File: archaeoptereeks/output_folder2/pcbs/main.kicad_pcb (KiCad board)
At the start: 2 copper layers, 246.9 x 153.3 mm, 118 parts

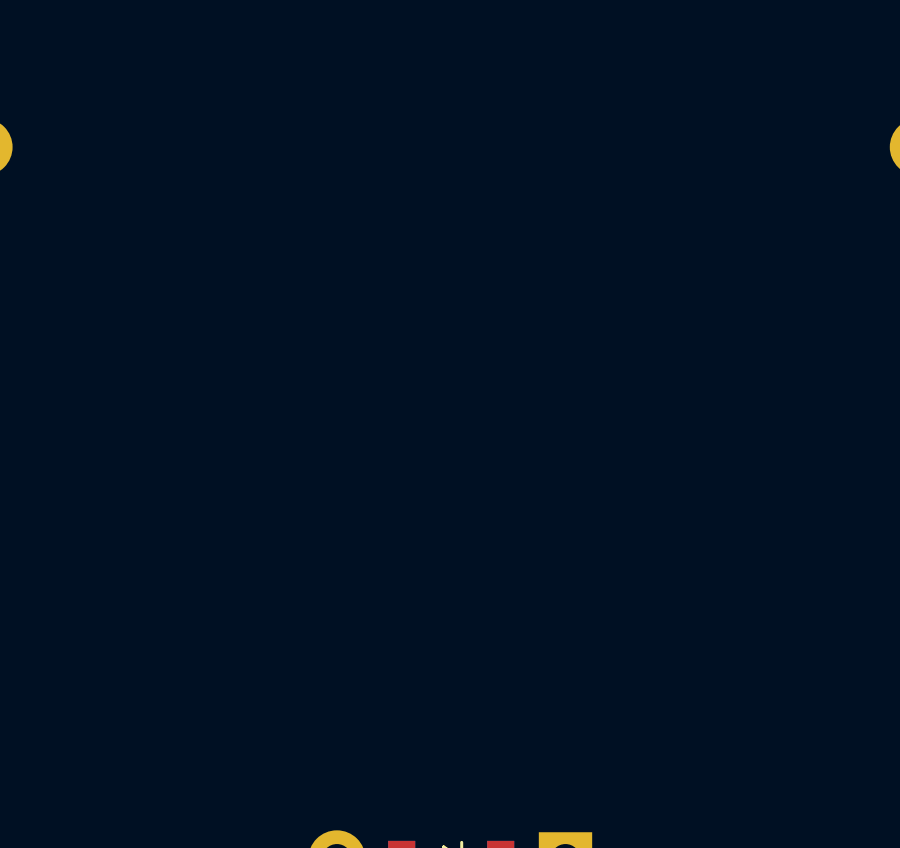
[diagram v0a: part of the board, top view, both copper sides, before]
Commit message: removing net and model reference from rotary_nosilk.js
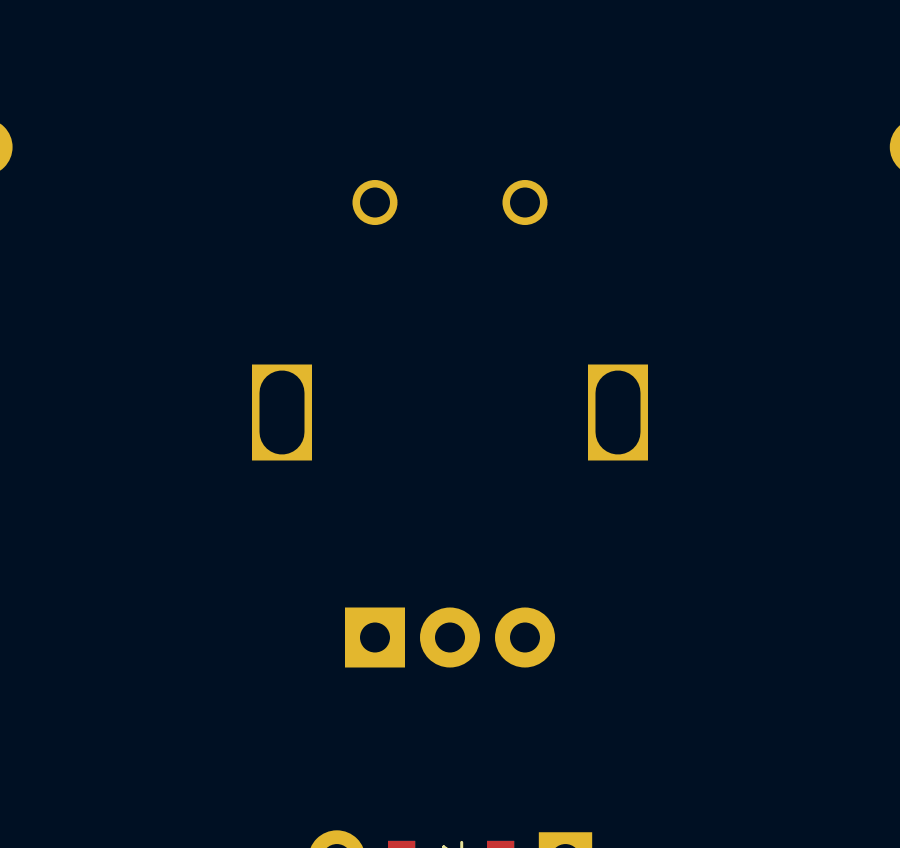
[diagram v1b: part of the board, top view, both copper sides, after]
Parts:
- added _1: , rotary_encoder, F.Cu at (186.7, 171.3)
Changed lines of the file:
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@@
         (pad 2 smd rect (at 3.1 1.85 -32) (size 1.8 1.1) (layers B.Cu B.Paste B.Mask) (net 56 "RST"))
     )
+        (module rotary_encoder (layer F.Cu)
+            (at 186.6593818 171.3311406 90)
+            (fp_text reference "_1" (at 0 0.5) (layer F.SilkS)
+                hide (effects (font (size 1 1) (thickness 0.15))))
+            (fp_text value "" (at 0 8.89) (layer F.Fab)
+                (effects (font (size 1 1) (thickness 0.15))))
+            (fp_line (start -3.12 -0.04) (end 2.88 -0.04) (layer F.Fab) (width 0.12))
+            (fp_line (start -0.12 -3.04) (end -0.12 2.96) (layer F.Fab) (width 0.12))
+            (fp_line (start -6.12 -4.74) (end -5.12 -5.84) (layer F.Fab) (width 0.12))
+            (fp_line (start -6.12 5.76) (end -6.12 -4.74) (layer F.Fab) (width 0.12))
+            (fp_line (start 5.88 5.76) (end -6.12 5.76) (layer F.Fab) (width 0.12))
+            (fp_line (start 5.88 -5.84) (end 5.88 5.76) (layer F.Fab) (width 0.12))
+            (fp_line (start -5.12 -5.84) (end 5.88 -5.84) (layer F.Fab) (width 0.12))
+            (fp_line (start -8.87 -6.89) (end 7.88 -6.89) (layer F.CrtYd) (width 0.05))
+            (fp_line (start -8.87 -6.89) (end -8.87 6.81) (layer F.CrtYd) (width 0.05))
+            (fp_line (start 7.88 6.81) (end 7.88 -6.89) (layer F.CrtYd) (width 0.05))
+            (fp_line (start 7.88 6.81) (end -8.87 6.81) (layer F.CrtYd) (width 0.05))
+            (fp_circle (center -0.12 -0.04) (end 2.88 -0.04) (layer F.Fab) (width 0.12))
+            (pad A thru_hole rect (at -7.62 -2.54 90) (size 2 2) (drill 1) (layers *.Cu *.Mask) (net 28 "C0"))
+            (pad C thru_hole circle (at -7.62 -0.04) (size 2 2) (drill 1) (layers *.Cu *.Mask) (net 32 "C1"))
+            (pad B thru_hole circle (at -7.62 2.46) (size 2 2) (drill 1) (layers *.Cu *.Mask) (net 55 "GND"))
+            (pad 1 thru_hole circle (at 6.88 -2.54) (size 1.5 1.5) (drill 1) (layers *.Cu *.Mask) (net 0 ""))
+            (pad 2 thru_hole circle (at 6.88 2.46) (size 1.5 1.5) (drill 1) (layers *.Cu *.Mask) (net 0 ""))
+            (pad "" thru_hole rect (at -0.12 -5.64 90) (size 3.2 2) (drill oval 2.8 1.5) (layers *.Cu *.Mask))
+            (pad "" thru_hole rect (at -0.12 5.56 90) (size 3.2 2) (drill oval 2.8 1.5) (layers *.Cu *.Mask))
+        )
     (module ComboDiode (layer F.Cu)
         (at 186.6593818 186.3311406 180)

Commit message: working on matrix layout and routing
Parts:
- removed D37, D38, D39: , ComboDiode
- removed LED37, LED38: , ceoloide:YS-SK6812MINI-E (per-key, reversible)
- removed S37, S38: , PG1350
- removed _1: , rotary_encoder
- moved S19 116.8 mm to (282.7, 219.9), turned to 160 degrees
- moved LED19 114.5 mm to (284.3, 215.4), turned to -20 degrees
- moved D19 101.3 mm to (273.9, 217.7), turned to 70 degrees
- moved S28 79.3 mm to (227.7, 190.6), turned to 180 degrees
- moved LED28 78.7 mm to (227.7, 185.9), turned to 0 degrees
- moved S22 78.2 mm to (267.3, 197.6), turned to 170 degrees
- moved LED22 77.6 mm to (268.1, 193.0), turned to -10 degrees
- moved D28 75.5 mm to (218.7, 191.6), turned to 90 degrees
- moved D22 75.0 mm to (258.2, 197.0), turned to 80 degrees
- moved S34 68.5 mm to (212.7, 211.6), turned to 180 degrees
- moved LED34 68.2 mm to (212.7, 206.9), turned to 0 degrees
- moved S25 67.8 mm to (249.2, 181.3), turned to 175 degrees
- moved LED25 67.2 mm to (249.6, 176.7), turned to -5 degrees
- moved D25 64.0 mm to (240.1, 181.6), turned to 85 degrees
- moved D34 63.6 mm to (203.7, 212.6), turned to 90 degrees
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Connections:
- D1 pad 1: R1 -> C1
- D10 pad 1: R1 -> C1
- D11 pad 1: R2 -> C0
- D12 pad 1: R3 -> P9
- D13 pad 1: R1 -> C1
- D14 pad 1: R2 -> C0
- D15 pad 1: R3 -> P9
- D16 pad 1: P9 -> C2
- D17 pad 1: P9 -> C2
- D18 pad 1: P9 -> C2
- D19 pad 1: P9 -> C1
- D19 pad 2: home_thumb -> mirror_pinky_bottom
- D2 pad 1: R2 -> C0
- D20 pad 1: R1 -> C0
- D20 pad 2: mirror_pinky_bottom -> mirror_pinky_home
- D21 pad 1: R2 -> P9
- D21 pad 2: mirror_pinky_home -> mirror_pinky_top
- D22 pad 1: R3 -> C1
- D22 pad 2: mirror_pinky_top -> mirror_ring_bottom
- D23 pad 1: R1 -> C0
- D23 pad 2: mirror_ring_bottom -> mirror_ring_home
- D24 pad 1: R2 -> P9
- D24 pad 2: mirror_ring_home -> mirror_ring_top
- D25 pad 1: R3 -> C1
- D25 pad 2: mirror_ring_top -> mirror_middle_bottom
- D26 pad 1: R1 -> C0
- D26 pad 2: mirror_middle_bottom -> mirror_middle_home
- D27 pad 1: R2 -> P9
- D27 pad 2: mirror_middle_home -> mirror_middle_top
- D28 pad 1: R3 -> C1
- D28 pad 2: mirror_middle_top -> mirror_index_bottom
- D29 pad 1: R1 -> C0
- D29 pad 2: mirror_index_bottom -> mirror_index_home
- D3 pad 1: R3 -> P9
- D30 pad 1: R2 -> P9
- D30 pad 2: mirror_index_home -> mirror_index_top
- D31 pad 1: R3 -> C1
- D31 pad 2: mirror_index_top -> mirror_inner_bottom
- D32 pad 1: R1 -> C0
- D32 pad 2: mirror_inner_bottom -> mirror_inner_home
- D33 pad 1: R2 -> P9
- D33 pad 2: mirror_inner_home -> mirror_inner_top
- D34 pad 1: R3 -> C2
- D34 pad 2: mirror_inner_top -> mirror_near_thumb
- D35 pad 1: P9 -> C2
- D35 pad 2: mirror_near_thumb -> mirror_home_thumb
- D36 pad 1: P9 -> C2
- D36 pad 2: mirror_home_thumb -> mirror_far_thumb
- D4 pad 1: R1 -> C1
- D5 pad 1: R2 -> C0
- D6 pad 1: R3 -> P9
- D7 pad 1: R1 -> C1
- D8 pad 1: R2 -> C0
- D9 pad 1: R3 -> P9
- LED18 pad 2: LED_20 -> LED_19
- LED18 pad 4: LED_19 -> LED_18
- LED19 pad 2: LED_19 -> LED_35
- LED19 pad 4: LED_18 -> LED_34
- LED20 pad 2: LED_37 -> LED_36
- LED20 pad 4: LED_36 -> LED_35
- LED21 pad 2: LED_38 -> (no net)
- LED22 pad 2: (no net) -> LED_34
- LED22 pad 4: LED_38 -> LED_33
- LED23 pad 2: LED_36 -> LED_33
- LED23 pad 4: LED_35 -> LED_32
- LED24 pad 2: LED_35 -> LED_32
- LED24 pad 4: LED_34 -> LED_31
- LED25 pad 2: LED_34 -> LED_29
- LED25 pad 4: LED_33 -> LED_28
- LED26 pad 2: LED_31 -> LED_30
- LED26 pad 4: LED_30 -> LED_29
- LED27 pad 2: LED_32 -> LED_31
- LED27 pad 4: LED_31 -> LED_30
- LED28 pad 2: LED_33 -> LED_28
- LED28 pad 4: LED_32 -> LED_27
- LED29 pad 2: LED_30 -> LED_27
- LED29 pad 4: LED_29 -> LED_26
- LED30 pad 2: LED_29 -> LED_26
- LED30 pad 4: LED_28 -> LED_25
- LED31 pad 2: LED_28 -> LED_23
- LED31 pad 4: LED_27 -> LED_22
- LED32 pad 2: LED_25 -> LED_24
- LED32 pad 4: LED_24 -> LED_23
- LED33 pad 2: LED_26 -> LED_25
- LED33 pad 4: LED_25 -> LED_24
- LED34 pad 2: LED_27 -> LED_22
- LED34 pad 4: LED_26 -> LED_21
- LED35 pad 2: LED_24 -> LED_21
- LED35 pad 4: LED_23 -> LED_20
- LED36 pad 2: LED_23 -> LED_20
- LED36 pad 4: LED_22 -> LED_19
- S1 pad 1: DAT -> R1
- S10 pad 1: CS -> R2
- S11 pad 1: CS -> R2
- S12 pad 1: CS -> R2
- S13 pad 1: R0 -> R3
- S14 pad 1: R0 -> R3
- S15 pad 1: R0 -> R3
- S16 pad 1: SDA -> R0
- S17 pad 1: SLC -> CS
- S18 pad 1: CS -> R2
- S19 pad 1: R0 -> P10
- S19 pad 2: home_thumb -> mirror_pinky_bottom
- S2 pad 1: DAT -> R1
- S20 pad 2: mirror_pinky_bottom -> mirror_pinky_home
- S21 pad 2: mirror_pinky_home -> mirror_pinky_top
- S22 pad 1: P10 -> P16
- S22 pad 2: mirror_pinky_top -> mirror_ring_bottom
- S23 pad 1: C0 -> P16
- S23 pad 2: mirror_ring_bottom -> mirror_ring_home
- S24 pad 1: C0 -> P16
- S24 pad 2: mirror_ring_home -> mirror_ring_top
- S25 pad 1: C0 -> C5
- S25 pad 2: mirror_ring_top -> mirror_middle_bottom
- S26 pad 1: C1 -> C5
- S26 pad 2: mirror_middle_bottom -> mirror_middle_home
- S27 pad 1: C1 -> C5
- S27 pad 2: mirror_middle_home -> mirror_middle_top
- S28 pad 1: C1 -> C4
- S28 pad 2: mirror_middle_top -> mirror_index_bottom
- S29 pad 1: C2 -> C4
- S29 pad 2: mirror_index_bottom -> mirror_index_home
- S3 pad 1: DAT -> R1
- S30 pad 1: C2 -> C4
- S30 pad 2: mirror_index_home -> mirror_index_top
- S31 pad 1: C2 -> C3
- S31 pad 2: mirror_index_top -> mirror_inner_bottom
- S32 pad 2: mirror_inner_bottom -> mirror_inner_home
- S33 pad 2: mirror_inner_home -> mirror_inner_top
- S34 pad 1: C3 -> P16
- S34 pad 2: mirror_inner_top -> mirror_near_thumb
- S35 pad 1: C4 -> C5
- S35 pad 2: mirror_near_thumb -> mirror_home_thumb
- S36 pad 1: C5 -> C4
- S36 pad 2: mirror_home_thumb -> mirror_far_thumb
- S4 pad 1: SDA -> R0
- S5 pad 1: SDA -> R0
- S6 pad 1: SDA -> R0
- S7 pad 1: SLC -> CS
- S8 pad 1: SLC -> CS
- S9 pad 1: SLC -> CS
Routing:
- net VCC: track 142.7 -> 977.2 mm, vias 38 -> 36
- net GND: track 142.7 -> 895.8 mm, vias 38 -> 37
- net R1: track 0.00 -> 415.3 mm
- net C0: track 0.00 -> 297.1 mm
- net C1: track 0.00 -> 257.3 mm
- net R0: track 0.00 -> 221.6 mm
- net R2: track 0.00 -> 210.1 mm, vias 0 -> 1
- net P9: track 0.00 -> 200.4 mm
- net R3: track 0.00 -> 159.5 mm
- net C3: track 0.00 -> 113.8 mm
- net LED: track 6.76 -> 119.5 mm
- net CS: track 0.00 -> 108.2 mm
- net C2: track 0.00 -> 76.2 mm
- net RST: track 0.00 -> 54.9 mm, vias 0 -> 1
- net LED_6: track 13.5 -> 57.0 mm, vias 2 -> 4
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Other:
- board size 246.9 x 153.3 mm -> 228.7 x 180.7 mm
- net class Default removed

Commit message: adding mounting holes and top plate
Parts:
- added H1: , mounting_hole, F.Cu at (98.7, 110.1)
- added H2: , mounting_hole, F.Cu at (274.7, 110.1)
- added H3: , mounting_hole, F.Cu at (160.4, 115.6)
- added H4: , mounting_hole, F.Cu at (212.9, 115.6)
- added H5: , mounting_hole, F.Cu at (89.3, 168.4)
- added H6: , mounting_hole, F.Cu at (284.0, 168.4)
- added H7: , mounting_hole, F.Cu at (177.4, 234.8)
- added H8: , mounting_hole, F.Cu at (195.9, 234.8)
- moved LED21 61.7 mm to (289.7, 118.4), turned to 12 degrees
- moved LED3 61.7 mm to (83.6, 118.4), turned to -12 degrees
- moved S19 61.7 mm to (298.6, 160.2), turned to -168 degrees
- moved S1 61.7 mm to (74.7, 160.2), turned to 168 degrees
- moved S21 61.3 mm to (290.7, 123.0), turned to -168 degrees
- moved S3 61.3 mm to (82.6, 123.0), turned to 168 degrees
- moved LED19 61.3 mm to (297.6, 155.6), turned to 12 degrees
- moved LED1 61.3 mm to (75.7, 155.6), turned to -12 degrees
- moved LED20 60.6 mm to (293.7, 137.0), turned to 12 degrees
- moved LED2 60.6 mm to (79.6, 137.0), turned to -12 degrees
- moved S20 60.6 mm to (294.7, 141.6), turned to -168 degrees
- moved S2 60.6 mm to (78.7, 141.6), turned to 168 degrees
- moved D1 57.0 mm to (83.3, 163.1), turned to 78 degrees
- moved D19 57.0 mm to (290.0, 163.1), turned to 102 degrees
- moved D21 56.3 mm to (282.1, 125.9), turned to 102 degrees
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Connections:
- LED21 pad 4: LED_37 -> LED_36
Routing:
- net VCC: track 977.2 -> 135.1 mm
- net GND: track 895.8 -> 135.1 mm, vias 37 -> 36
- net C0: track 297.1 -> 0.00 mm
- net R1: track 415.3 -> 121.9 mm
- net C1: track 257.3 -> 0.00 mm
- net R0: track 221.6 -> 0.00 mm
- net P9: track 200.4 -> 0.00 mm
- net R3: track 159.5 -> 0.00 mm
- net C3: track 113.8 -> 0.00 mm
- net LED: track 119.5 -> 6.76 mm
- net CS: track 108.2 -> 0.00 mm
- net R2: track 210.1 -> 121.8 mm, vias 1 -> 0
- net C2: track 76.2 -> 0.00 mm
- net RST: track 54.9 -> 0.00 mm, vias 1 -> 0
- net far_thumb: track 2.16 -> 50.9 mm
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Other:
- board size 228.7 x 180.7 mm -> 246.9 x 153.3 mm
- net class Default added: clearance 0.2, trace_width 0.25, via_dia 0.8, via_drill 0.4
- board text added: "JLCJLCJLCJLC"

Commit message: adjusting traces for mount holes
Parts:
- moved LED21 61.7 mm to (297.3, 179.7), turned to -20 degrees
- moved LED3 61.7 mm to (122.5, 70.5), turned to -44 degrees
- moved S19 61.7 mm to (282.7, 219.9), turned to 160 degrees
- moved S1 61.7 mm to (92.8, 101.2), turned to 136 degrees
- moved S21 61.3 mm to (295.7, 184.1), turned to 160 degrees
- moved S3 61.3 mm to (119.2, 73.9), turned to 136 degrees
- moved LED19 61.3 mm to (284.3, 215.4), turned to -20 degrees
- moved LED1 61.3 mm to (96.1, 97.8), turned to -44 degrees
- moved LED20 60.6 mm to (290.8, 197.6), turned to -20 degrees
- moved LED2 60.6 mm to (109.3, 84.2), turned to -44 degrees
- moved S20 60.6 mm to (289.2, 202.0), turned to 160 degrees
- moved S2 60.6 mm to (106.0, 87.5), turned to 136 degrees
- moved D1 57.0 mm to (98.6, 108.2), turned to 46 degrees
- moved D19 57.0 mm to (273.9, 217.7), turned to 70 degrees
- moved H2 56.4 mm to (288.9, 164.7), turned to -20 degrees
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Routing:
- net GND: track 135.1 -> 1568.9 mm, vias 36 -> 40
- net VCC: track 135.1 -> 1459.3 mm, vias 36 -> 37
- net C0: track 0.00 -> 563.7 mm
- net C1: track 0.00 -> 488.4 mm
- net P9: track 0.00 -> 354.8 mm
- net R0: track 0.00 -> 333.4 mm
- net P16: track 0.00 -> 310.2 mm
- net CS: track 0.00 -> 297.4 mm
- net C2: track 0.00 -> 293.4 mm
- net C5: track 0.00 -> 271.6 mm
- net C4: track 0.00 -> 269.8 mm
- net P10: track 50.9 -> 251.0 mm
- net C3: track 0.00 -> 185.3 mm
- net R2: track 121.8 -> 299.4 mm, vias 0 -> 1
- net R3: track 0.00 -> 165.4 mm
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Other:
- board size 246.9 x 153.3 mm -> 228.7 x 180.7 mm
- net class Default removed

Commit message: playing with ergogen and working on silk drawings
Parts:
- moved LED21 61.7 mm to (289.7, 118.4), turned to 12 degrees
- moved LED3 61.7 mm to (83.6, 118.4), turned to -12 degrees
- moved S19 61.7 mm to (298.6, 160.2), turned to -168 degrees
- moved S1 61.7 mm to (74.7, 160.2), turned to 168 degrees
- moved S21 61.3 mm to (290.7, 123.0), turned to -168 degrees
- moved S3 61.3 mm to (82.6, 123.0), turned to 168 degrees
- moved LED19 61.3 mm to (297.6, 155.6), turned to 12 degrees
- moved LED1 61.3 mm to (75.7, 155.6), turned to -12 degrees
- moved LED20 60.6 mm to (293.7, 137.0), turned to 12 degrees
- moved LED2 60.6 mm to (79.6, 137.0), turned to -12 degrees
- moved S20 60.6 mm to (294.7, 141.6), turned to -168 degrees
- moved S2 60.6 mm to (78.7, 141.6), turned to 168 degrees
- moved D1 57.0 mm to (83.3, 163.1), turned to 78 degrees
- moved D19 57.0 mm to (290.0, 163.1), turned to 102 degrees
- moved H2 56.4 mm to (274.7, 110.1), turned to 12 degrees
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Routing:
- net GND: track 1568.9 -> 135.1 mm, vias 40 -> 36
- net VCC: track 1459.3 -> 135.1 mm, vias 37 -> 36
- net C0: track 563.7 -> 0.00 mm
- net C1: track 488.4 -> 0.00 mm
- net P9: track 354.8 -> 0.00 mm
- net R0: track 333.4 -> 0.00 mm
- net P16: track 310.2 -> 0.00 mm
- net CS: track 297.4 -> 0.00 mm
- net C2: track 293.4 -> 0.00 mm
- net C5: track 271.6 -> 0.00 mm
- net C4: track 269.8 -> 0.00 mm
- net P10: track 251.0 -> 50.9 mm
- net C3: track 185.3 -> 0.00 mm
- net R2: track 299.4 -> 121.8 mm, vias 1 -> 0
- net R3: track 165.4 -> 0.00 mm
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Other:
- board size 228.7 x 180.7 mm -> 246.9 x 153.3 mm
- net class Default added: clearance 0.2, trace_width 0.25, via_dia 0.8, via_drill 0.4
